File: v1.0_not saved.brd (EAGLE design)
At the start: 184.8 x 101.3 mm, 248 parts, among them J1 DC-044-A, J2 MICROSD-9P, J3 2p-2.54, J4 2p-2.54, J5 16p-2.54, J6 16p-2.54, J7 2x3p-2.54, J8 2p-2.54, Q2 SSM3J328R,LF, Q3 6pF@32.7680kHz, Q4 BSS138W-7-F, Q5 SSM3J328R,LF, SW1 SW-200D, SW2 SW-200D, SW3 SW-200D, SW4 SW-200D, SW5 SW-200D, SW6 SW-200D, SW7 SW-200D, SW8 SW-200D, U1 MCP23017-E/SO, U10 74HC139N, U11 BZX84C30, U12 SP483ECN-L, U13 FT232RL-SSOP28, U14 FT232RL-SSOP28, U15 FT232RL-SSOP28, U2 MCP79412-I/SN, U3 LOPY, U5 FT232RL-SSOP28, U6 FT232RL-SSOP28, U7 2x14p-2.54, U8 BR24G32-3, Y2 12MHZ

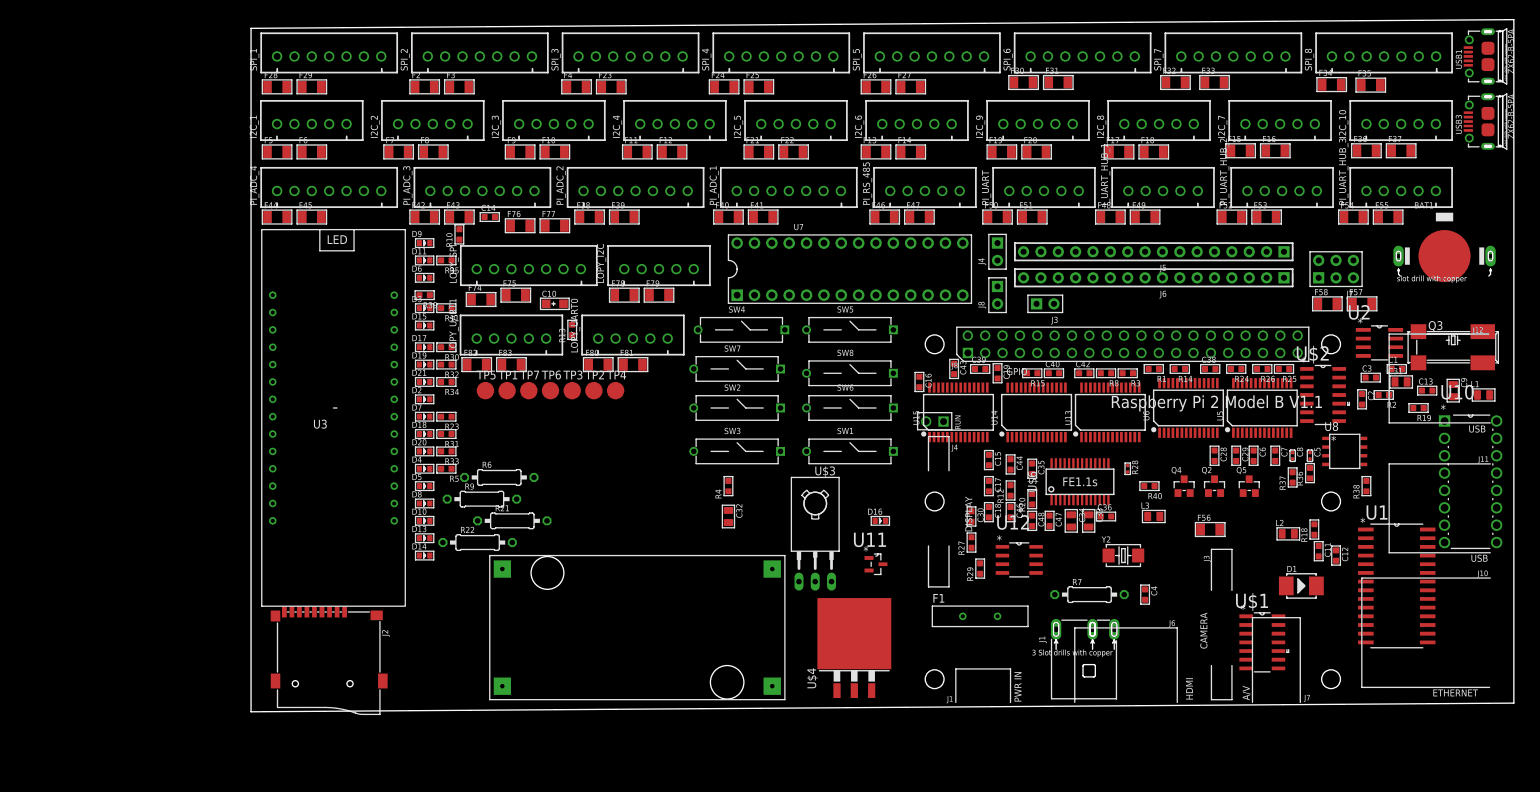
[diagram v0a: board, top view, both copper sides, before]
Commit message: started double checking board position against schematics
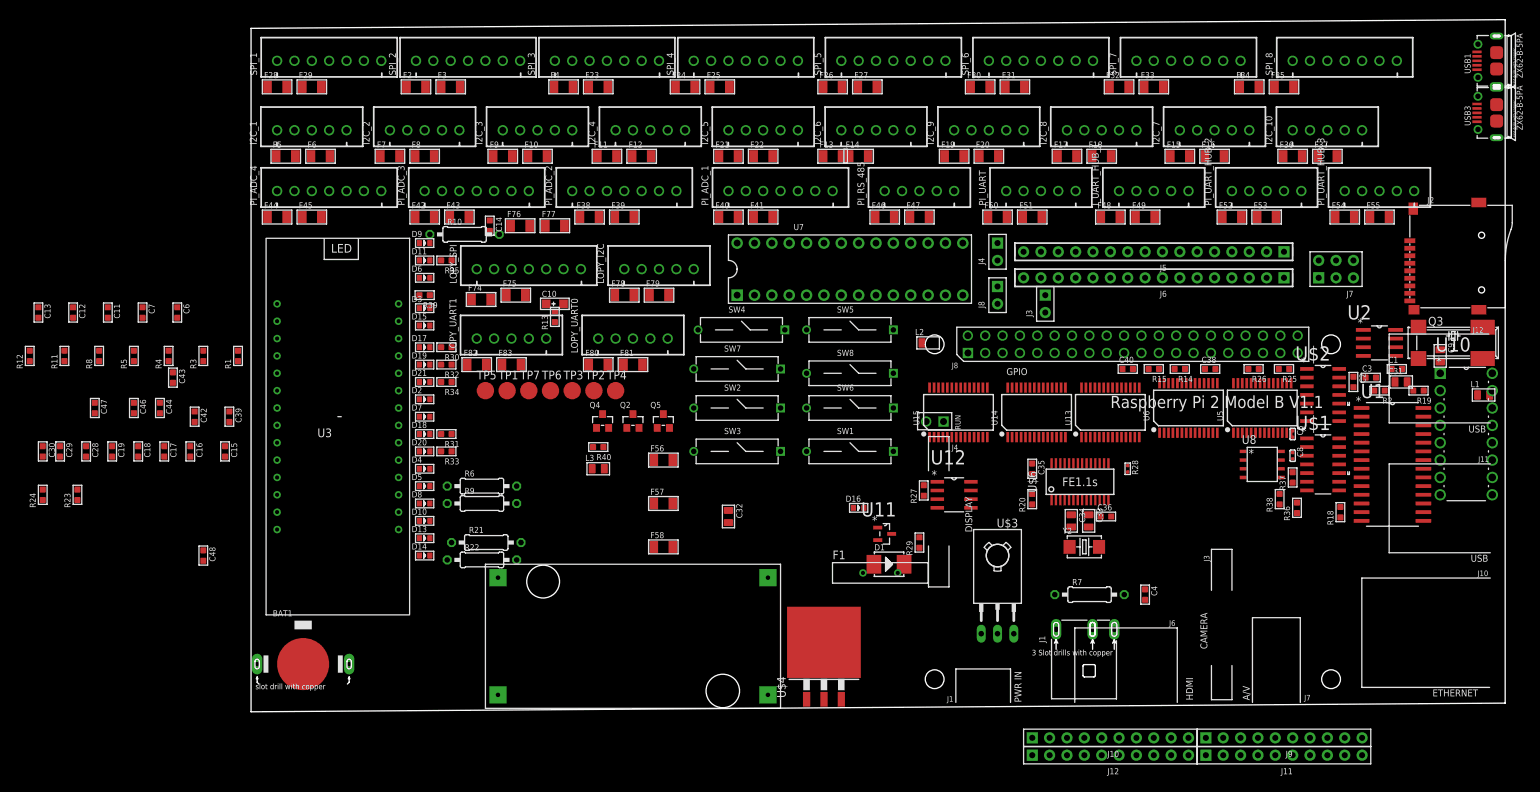
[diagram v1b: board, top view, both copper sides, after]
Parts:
- added J10, J11, J12, J9: 10p-2.54, Seeed-Connector:H10-2.54
- R10: device Seeed-Resistor:R0603 -> Seeed-Resistor:PR-D2.3XL6.5MM
- moved C13 203.5 mm to (-31.1, 58.4), turned to 0 degrees
- moved C12 188.2 mm to (-26.0, 58.4)
- moved C11 180.6 mm to (-21.0, 58.4)
- moved BAT1 177.4 mm to (7.62, 6.99)
- moved R24 175.6 mm to (-30.5, 31.8), turned to 0 degrees
- moved C29 172.1 mm to (-27.9, 38.1)
- moved C7 167.1 mm to (-15.9, 58.4)
- moved J2 166.5 mm to (169.5, 66.7), turned to 0 degrees
- moved C28 165.1 mm to (-24.1, 38.1)
- moved C6 158.9 mm to (-10.8, 58.4)
- moved R8 147.3 mm to (-22.2, 52.1), turned to 0 degrees
- moved R12 144.9 mm to (-32.4, 52.1)
- moved C47 140.7 mm to (-22.9, 44.5)
- moved C30 136.2 mm to (-30.5, 38.1)
- moved R3 135.3 mm to (-6.99, 52.1), turned to 0 degrees
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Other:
- board size 184.8 x 101.3 mm -> 183.5 x 101.3 mm
